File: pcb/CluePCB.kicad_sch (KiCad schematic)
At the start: 7 parts, among them U1 LoRa, U2 GPS, U3 Dragontail, U4 PowerBoost500, U5 Drag3V

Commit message: first draft on schematic
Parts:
- removed R1: 2.2k, Resistor_THT:R_Axial_DIN0204_L3.6mm_D1.6mm_P5.08mm_Horizontal, symbol Device:R
- removed R2: 3.3k, Resistor_THT:R_Axial_DIN0204_L3.6mm_D1.6mm_P5.08mm_Horizontal, symbol Device:R
- removed U1: LoRa, HABET_Lib:LoRa, symbol HABET_Lib:LoRa
- removed U2: GPS, HABET_Lib:GPS, symbol HABET_Lib:GPS
- removed U3: Dragontail, HABET_Lib:Dragontail, symbol HABET_Lib:Dragontail
- removed U4: PowerBoost500, HABET_Lib:Powerboost500, symbol HABET_Lib:PowerBoost500
- removed U5: Drag3V, HABET_Lib:Dragon3V, symbol HABET_Lib:Drag3V
- added BT?: Battery_Cell, symbol Device:Battery_Cell
- added J? (x3): Conn_01x02, symbol Connector_Generic:Conn_01x02
- added SW?: SW_SPST, symbol Switch:SW_SPST
- added U?: Sparkfun_PRT-14411, symbol HAR:Sparkfun_PRT-14411
- added U?: Sparkfun_Microbit_BOB-16446, symbol HAR:Sparkfun_Microbit_BOB-16446
- added U?: AP2112K-3.3, Package_TO_SOT_SMD:SOT-23-5, symbol Regulator_Linear:AP2112K-3.3
- added U?: Adafruit_RFM96W-3073, symbol HAR:Adafruit_RFM96W-3073
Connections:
- new net: J?.1 (Pin_1), U?.3 (EN)
- new net: BT?.1 (+), U?.8 (BATT+)
- new net: SW?.1 (A), U?.1 (EXT_SW+)
- new net: SW?.2 (B), U?.2 (EXT_SW-)
- new net: J?.2 (Pin_2), U?.3 (5VIN+)
- new net: U?.1 (VIN), U?.6 (5VOUT+)
- new net: U?.13 (SCK), U?.4 (SCK)
- new net: U?.14 (MISO), U?.5 (MISO)
- new net: U?.15 (MOSI), U?.6 (MOSI)
- new net: U?.16 (GP16), U?.7 (CS)
- new net: U?.2 (AIN2), U?.8 (RST)
- new net: U?.1 (VIN), U?.23 (3V3), U?.5 (VOUT)
- new net: U?.3 (G0), U?.8 (GPIO)
- new net GND: BT?.2 (-), J?.1 (Pin_1), J?.2 (Pin_2), U?.2 (GND), U?.2 (GND), U?.21 (GND), U?.22 (GND), U?.4 (5VIN-), U?.7 (5VOUT-), U?.9 (BATT-)
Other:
- company: (none) -> Make to Innovate
- title: (none) -> High Altitude Reporter (HAR)

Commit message: First take on PCB
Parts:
- added C1, C2: 0.1uF, Capacitor_THT:C_Rect_L7.0mm_W4.5mm_P5.00mm, symbol Device:C
- BT1: renamed from BT?; footprint (none) -> Battery:BatteryHolder_Keystone_1042_1x18650
- J1, J2, J3: renamed from J?; footprint (none) -> Connector_PinHeader_2.54mm:PinHeader_1x02_P2.54mm_Vertical
- SW1: renamed from SW?; footprint (none) -> Connector_PinHeader_2.54mm:PinHeader_1x02_P2.54mm_Vertical
- U1: renamed from U?; footprint (none) -> HAR:Sparkfun Boost BOB
- U3: renamed from U?; footprint (none) -> HAR:Sparkfun Microbit BOB
- U4: renamed from U?; footprint (none) -> HAR:Adafruit LoRa BOB
- gave numbers to parts that had none: 1
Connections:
- net GND: now also C1.2, C2.2
- net at U1.6 (5VOUT+), U2.1 (VIN): now also C1.1
- net at U2.5 (VOUT), U3.23 (3V3), U4.1 (VIN): now also C2.1

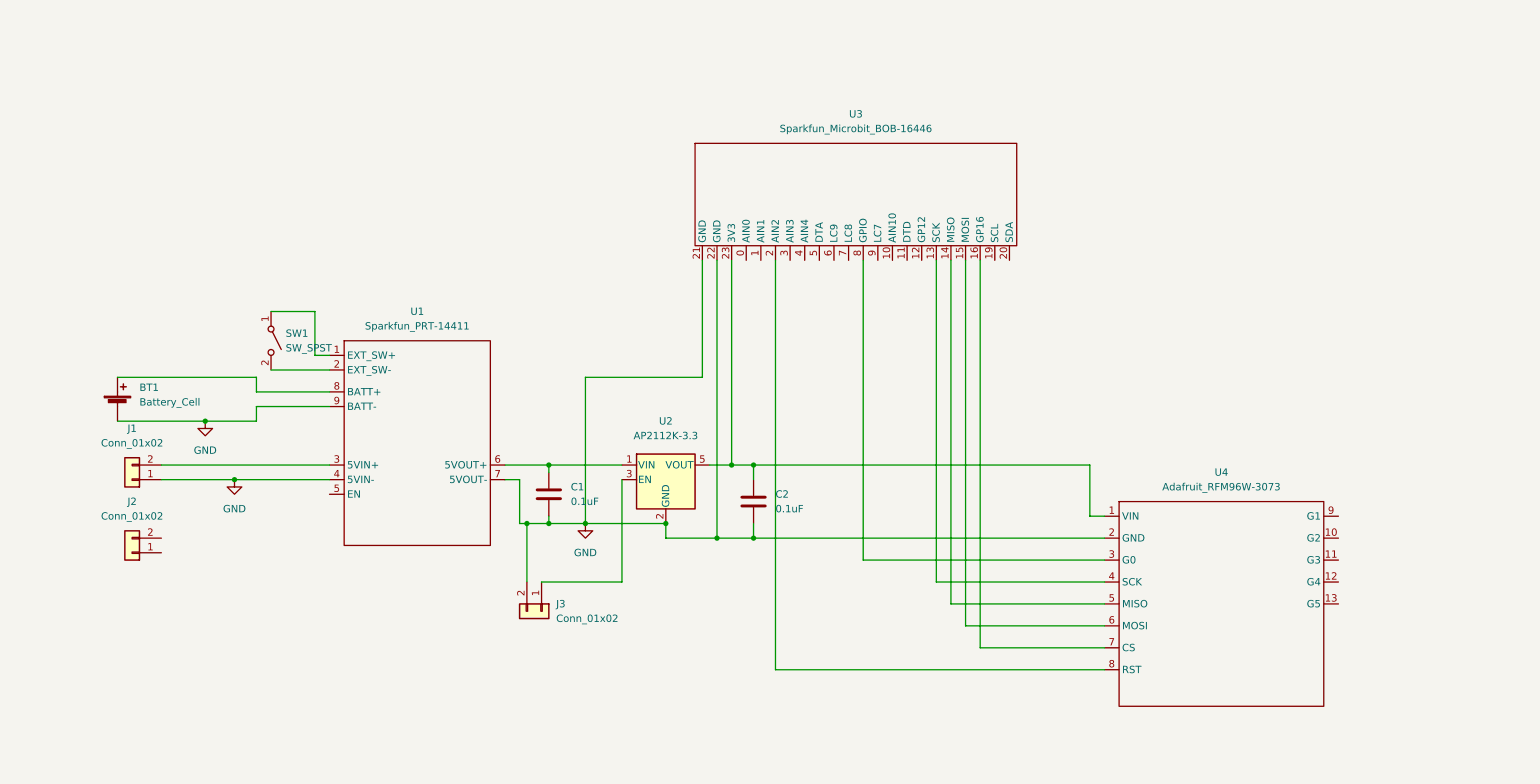
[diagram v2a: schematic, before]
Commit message: Fixed some Footprints
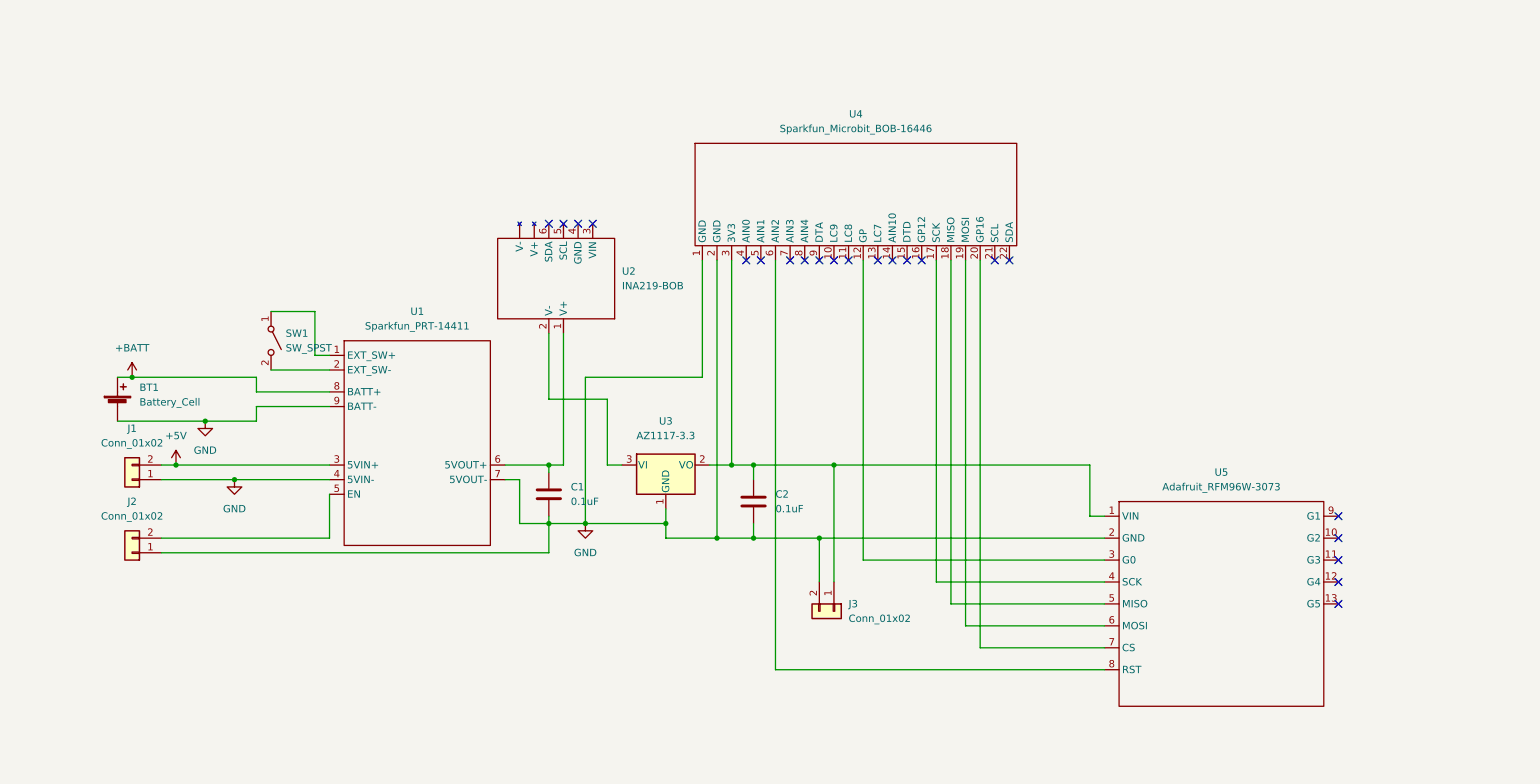
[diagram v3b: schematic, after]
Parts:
- removed U2: AP2112K-3.3, Package_TO_SOT_SMD:SOT-23-5, symbol Regulator_Linear:AP2112K-3.3
- added U2: INA219-BOB, HAR:INA219, symbol HAR:INA219-BOB
- added U3: AZ1117-3.3, symbol Regulator_Linear:AZ1117-3.3
- renumbered U3 to U4, U4 to U5
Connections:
- net GND: now also J2.1 (Pin_1), U4.1 (GND), U4.2 (GND), U3.1 (GND); no longer U4.21 (GND), U4.22 (GND)
- net at J3.1 (Pin_1): now also C2.1, U4.3 (3V3), U5.1 (VIN), U3.2 (VO)
- net +BATT: now reaches BT1.1 (+), U1.8 (BATT+)
- net +5V: now reaches J1.2 (Pin_2), U1.3 (5VIN+)
- net at U1.5 (EN): now also J2.2 (Pin_2)
- net at C1.1, U1.6 (5VOUT+): now also U2.1 (V+)
- net at U4.12 (GP): now also U5.3 (G0)
- net at U4.13 (LC7): no longer U5.4 (SCK)
- net at U4.14 (AIN10): no longer U5.5 (MISO)
- net at U4.15 (DTD): no longer U5.6 (MOSI)
- net at U4.16 (GP12): no longer U5.7 (CS)
- net at U4.19 (MOSI): now also U5.6 (MOSI)
- net at U5.8 (RST): now also U4.6 (AIN2); no longer U4.2 (AIN2)
- net at U4.20 (GP16): now also U5.7 (CS)
- net at U4.8 (AIN4): no longer U5.3 (G0)
- new net: U2.2 (V-), U3.3 (VI)
- new net: U4.17 (SCK), U5.4 (SCK)
- new net: U4.18 (MISO), U5.5 (MISO)
- no-connect marks 0 -> 22
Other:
- moved on the sheet: J3

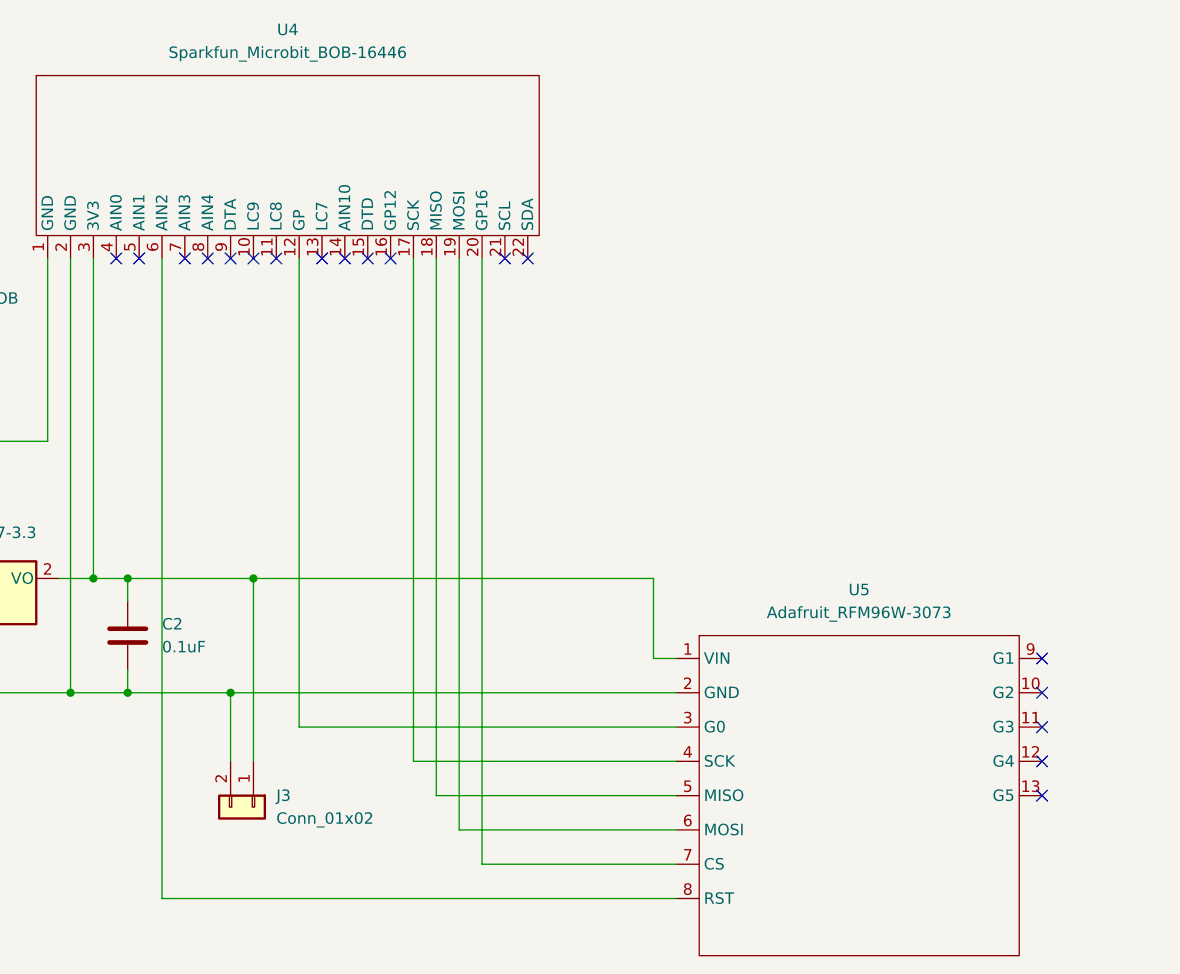
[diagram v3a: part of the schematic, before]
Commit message: 1st draft on board
Board ready for first review. Added 3D parts into repo. LoRa does need some work for mounting holes
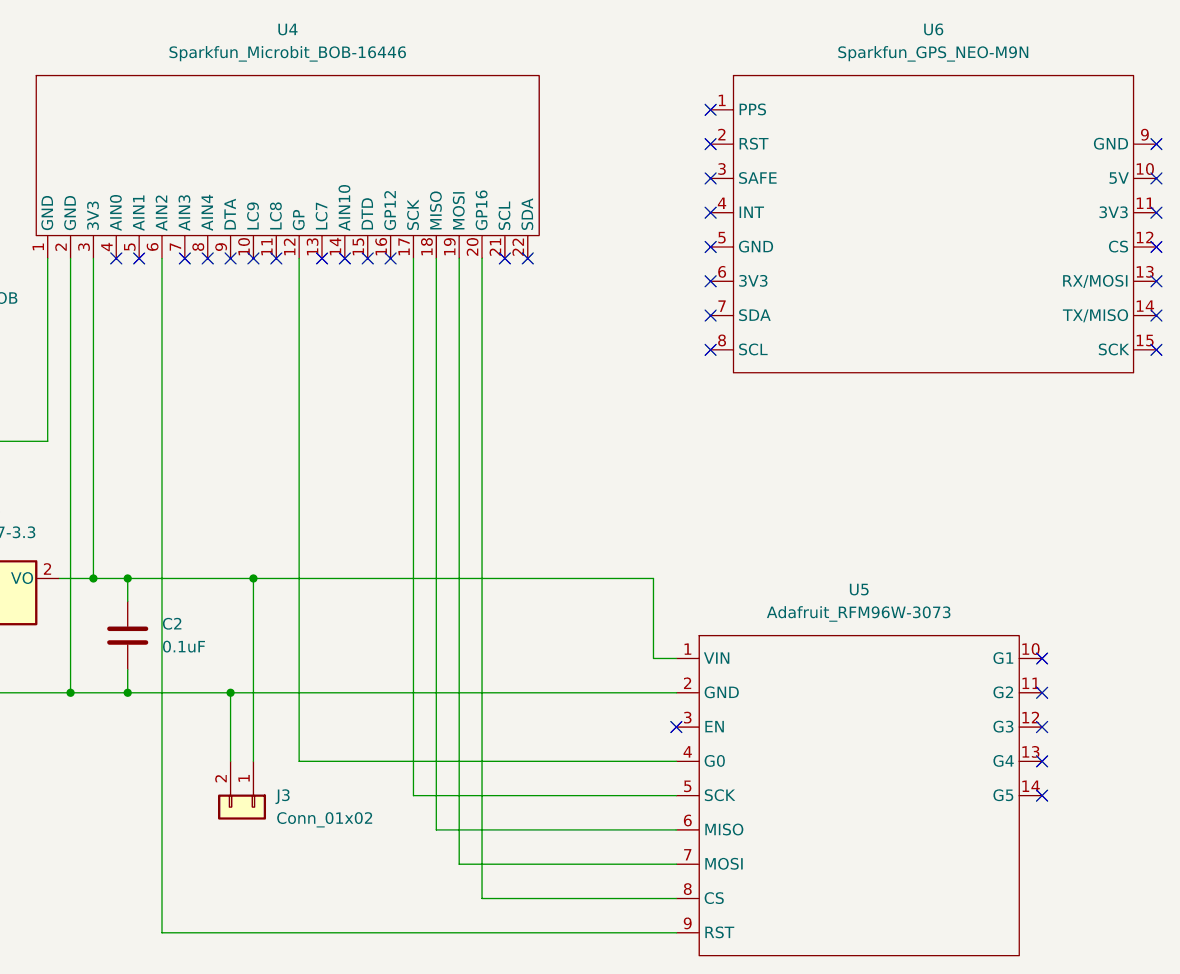
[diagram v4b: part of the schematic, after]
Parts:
- added U6: Sparkfun_GPS_NEO-M9N, HAR:Sparkfun GPS NEO M9N, symbol HAR:Sparkfun_GPS_NEO-M9N
- U3: footprint (none) -> Package_TO_SOT_SMD:TO-252-2
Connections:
- net at U4.12 (GP): now also U5.4 (G0); no longer U5.3 (G0)
- net at U4.17 (SCK): now also U5.5 (SCK); no longer U5.4 (SCK)
- net at U4.18 (MISO): now also U5.6 (MISO); no longer U5.5 (MISO)
- net at U4.19 (MOSI): now also U5.7 (MOSI); no longer U5.6 (MOSI)
- net at U4.20 (GP16): now also U5.8 (CS); no longer U5.7 (CS)
- net at U4.6 (AIN2): now also U5.9 (RST); no longer U5.8 (RST)
- no-connect marks 22 -> 38

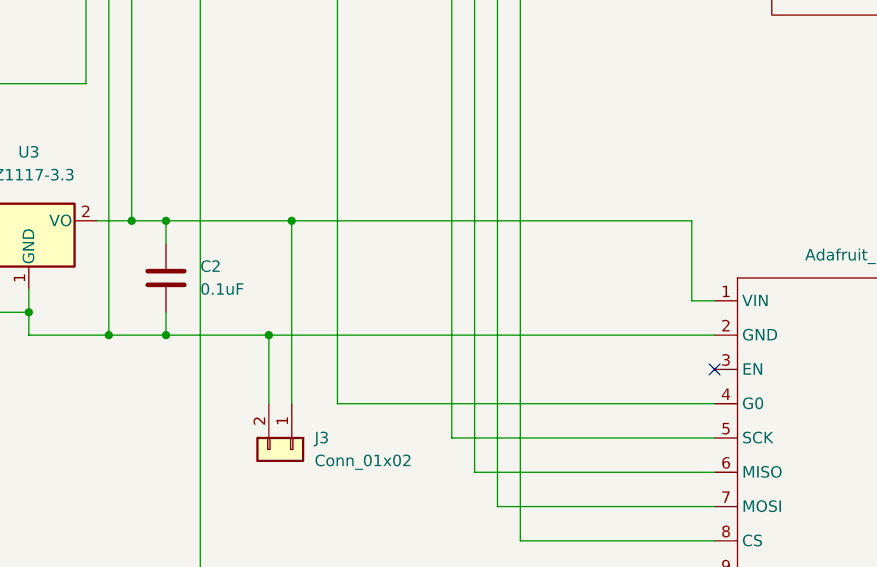
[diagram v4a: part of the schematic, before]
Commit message: Updated LoRa, started routing
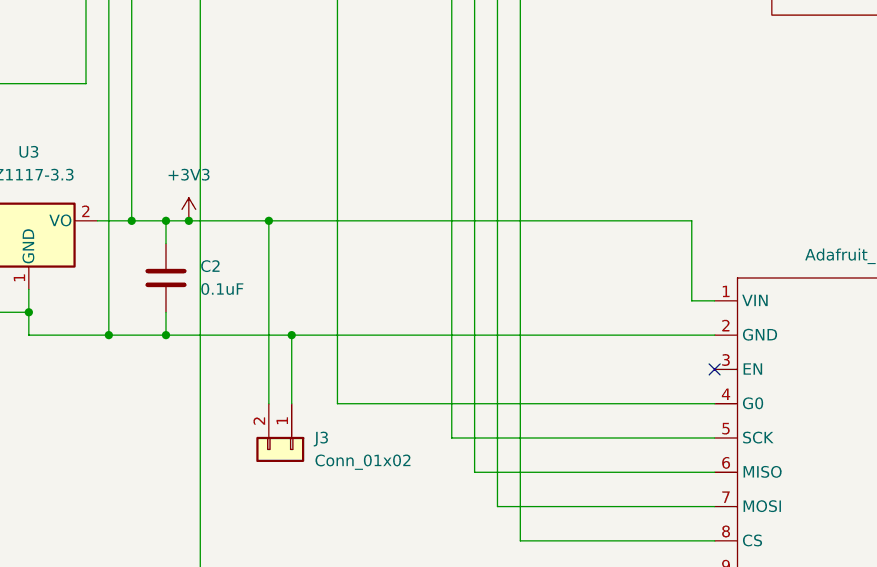
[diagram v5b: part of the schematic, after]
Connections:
- net GND: now also J3.1 (Pin_1); no longer J3.2 (Pin_2)
- net +3V3: now reaches C2.1, U3.2 (VO), U4.3 (3V3), U5.1 (VIN)
- net +3V3: now also J3.2 (Pin_2); no longer J3.1 (Pin_1)
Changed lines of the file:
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@@
   (junction (at 151.13 111.76) (diameter 0) (color 0 0 0 0)
   )
-  (junction (at 171.45 99.06) (diameter 0) (color 0 0 0 0)
+  (junction (at 160.02 99.06) (diameter 0) (color 0 0 0 0)
+  )
+  (junction (at 168.91 99.06) (diameter 0) (color 0 0 0 0)
   )
   (junction (at 142.24 109.22) (diameter 0) (color 0 0 0 0)
@@
   (junction (at 121.92 109.22) (diameter 0) (color 0 0 0 0)
   )
+  (junction (at 171.45 111.76) (diameter 0) (color 0 0 0 0)
+  )
   (junction (at 67.31 101.6) (diameter 0) (color 0 0 0 0)
-  )
-  (junction (at 168.91 111.76) (diameter 0) (color 0 0 0 0)
   )
   (junction (at 153.67 99.06) (diameter 0) (color 0 0 0 0)
@@
     (stroke (width 0) (type default) (color 0 0 0 0))
   )
+  (wire (pts (xy 168.91 99.06) (xy 215.9 99.06))
+    (stroke (width 0) (type default) (color 0 0 0 0))
+  )
   (wire (pts (xy 132.08 87.63) (xy 132.08 99.06))
     (stroke (width 0) (type default) (color 0 0 0 0))
@@
     (stroke (width 0) (type default) (color 0 0 0 0))
   )
-  (wire (pts (xy 168.91 119.38) (xy 168.91 111.76))
+  (wire (pts (xy 171.45 111.76) (xy 171.45 119.38))
     (stroke (width 0) (type default) (color 0 0 0 0))
   )
@@
     (stroke (width 0) (type default) (color 0 0 0 0))
   )
-  (wire (pts (xy 168.91 111.76) (xy 218.44 111.76))
+  (wire (pts (xy 157.48 111.76) (xy 171.45 111.76))
     (stroke (width 0) (type default) (color 0 0 0 0))
   )
@@
     (stroke (width 0) (type default) (color 0 0 0 0))
   )
-  (wire (pts (xy 171.45 99.06) (xy 215.9 99.06))
-    (stroke (width 0) (type default) (color 0 0 0 0))
-  )
   (wire (pts (xy 142.24 106.68) (xy 142.24 109.22))
     (stroke (width 0) (type default) (color 0 0 0 0))
@@
     (stroke (width 0) (type default) (color 0 0 0 0))
   )
+  (wire (pts (xy 171.45 111.76) (xy 218.44 111.76))
+    (stroke (width 0) (type default) (color 0 0 0 0))
+  )
   (wire (pts (xy 142.24 109.22) (xy 142.24 111.76))
     (stroke (width 0) (type default) (color 0 0 0 0))
@@
     (stroke (width 0) (type default) (color 0 0 0 0))
   )
+  (wire (pts (xy 168.91 99.06) (xy 168.91 119.38))
+    (stroke (width 0) (type default) (color 0 0 0 0))
+  )
   (wire (pts (xy 157.48 111.76) (xy 151.13 111.76))
     (stroke (width 0) (type default) (color 0 0 0 0))
@@
     (stroke (width 0) (type default) (color 0 0 0 0))
   )
-  (wire (pts (xy 157.48 111.76) (xy 168.91 111.76))
-    (stroke (width 0) (type default) (color 0 0 0 0))
-  )
   (wire (pts (xy 153.67 63.5) (xy 153.67 99.06))
     (stroke (width 0) (type default) (color 0 0 0 0))
@@
     (stroke (width 0) (type default) (color 0 0 0 0))
   )
-  (wire (pts (xy 157.48 99.06) (xy 171.45 99.06))
+  (wire (pts (xy 157.48 99.06) (xy 160.02 99.06))
     (stroke (width 0) (type default) (color 0 0 0 0))
   )
@@
     (stroke (width 0) (type default) (color 0 0 0 0))
   )
+  (wire (pts (xy 160.02 99.06) (xy 168.91 99.06))
+    (stroke (width 0) (type default) (color 0 0 0 0))
+  )
   (wire (pts (xy 71.12 83.82) (xy 71.12 86.36))
     (stroke (width 0) (type default) (color 0 0 0 0))
@@
   )
   (wire (pts (xy 157.48 99.06) (xy 157.48 101.6))
-    (stroke (width 0) (type default) (color 0 0 0 0))
-  )
-  (wire (pts (xy 171.45 99.06) (xy 171.45 119.38))
     (stroke (width 0) (type default) (color 0 0 0 0))
   )
@@
     (pin "1")
   )
+  (symbol (lib_id "power:+3V3") (at 160.02 99.06 0) (unit 1)
+    (in_bom yes) (on_board yes) (fields_autoplaced)
+    (property "Reference" "#PWR0101" (id 0) (at 160.02 102.87 0)
+      (effects (font (size 1.27 1.27)) hide)
+    )
+    (property "Value" "+3V3" (id 1) (at 160.02 93.98 0))
+    (property "Footprint" "" (id 2) (at 160.02 99.06 0)
+      (effects (font (size 1.27 1.27)) hide)
+    )
+    (property "Datasheet" "" (id 3) (at 160.02 99.06 0)
+      (effects (font (size 1.27 1.27)) hide)
+    )
+    (pin "1")
+  )
   (symbol (lib_id "HAR:Sparkfun_GPS_NEO-M9N") (at 246.38 59.69 0) (unit 1)
     (in_bom yes) (on_board yes) (fields_autoplaced)
@@
       (reference "#PWR05") (unit 1) (value "GND") (footprint "")
     )
+    (path "/45746010-0fb1-4548-9da6-cb3f04f25368"
+      (reference "#PWR0101") (unit 1) (value "+3V3") (footprint "")
+    )
     (path "/00cba8a2-a55e-474a-8579-54c3cf8b08cf"
